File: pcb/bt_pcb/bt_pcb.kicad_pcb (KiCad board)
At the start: 4 copper layers, 180 x 70 mm, 219 parts, among them IC1 LTC3621EMS8E-25#PBF, IC2 ADAU1961WBCPZ-R7, IC3 STM32H750VBT6, IC4 STM32H523CEU6, IC5 W25Q512JVEIM, J1 Conn_01x02, J10 Conn_01x03, J11 Conn_01x03, J12 Conn_01x05, J13 Conn_01x05, J14 Conn_01x05, J15 ReanNYS216G, J16 ReanNYS216G, J17 ReanNYS216G, J18 ReanNYS216G, J2 694106301002, J3 Conn_01x01, J4 Conn_01x01, J5 Conn_01x03, J6 Conn_01x03, J7 ER-OLEDM0383-1-SPI_Conn_01x10, J8 Conn_01x03, J9 USB_C_Receptacle_USB2.0_16P, SW1 RotaryEncoder_Switch, SW10 SW_Push, SW11 SW_Push, SW2 SW_Push, SW3 SW_Push, SW4 SW_Push, SW5 SW_Push, SW6 SW_Push, SW7 SW_Push, SW8 SW_Push, SW9 SW_Push, U1 TLV76133DCY, U2 TLV76133DCY, U3 MCP6004, U4 MCP6004

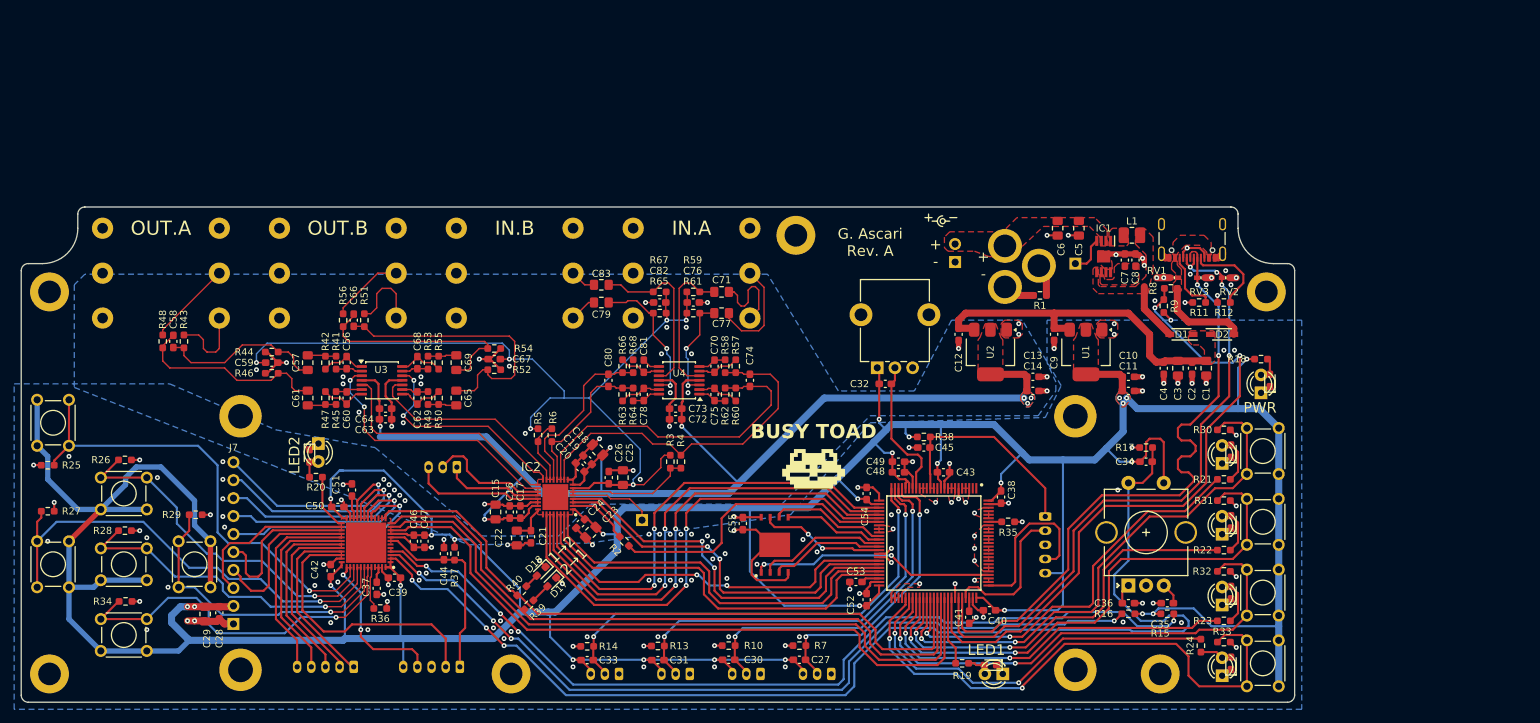
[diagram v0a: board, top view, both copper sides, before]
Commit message: redo of power supply
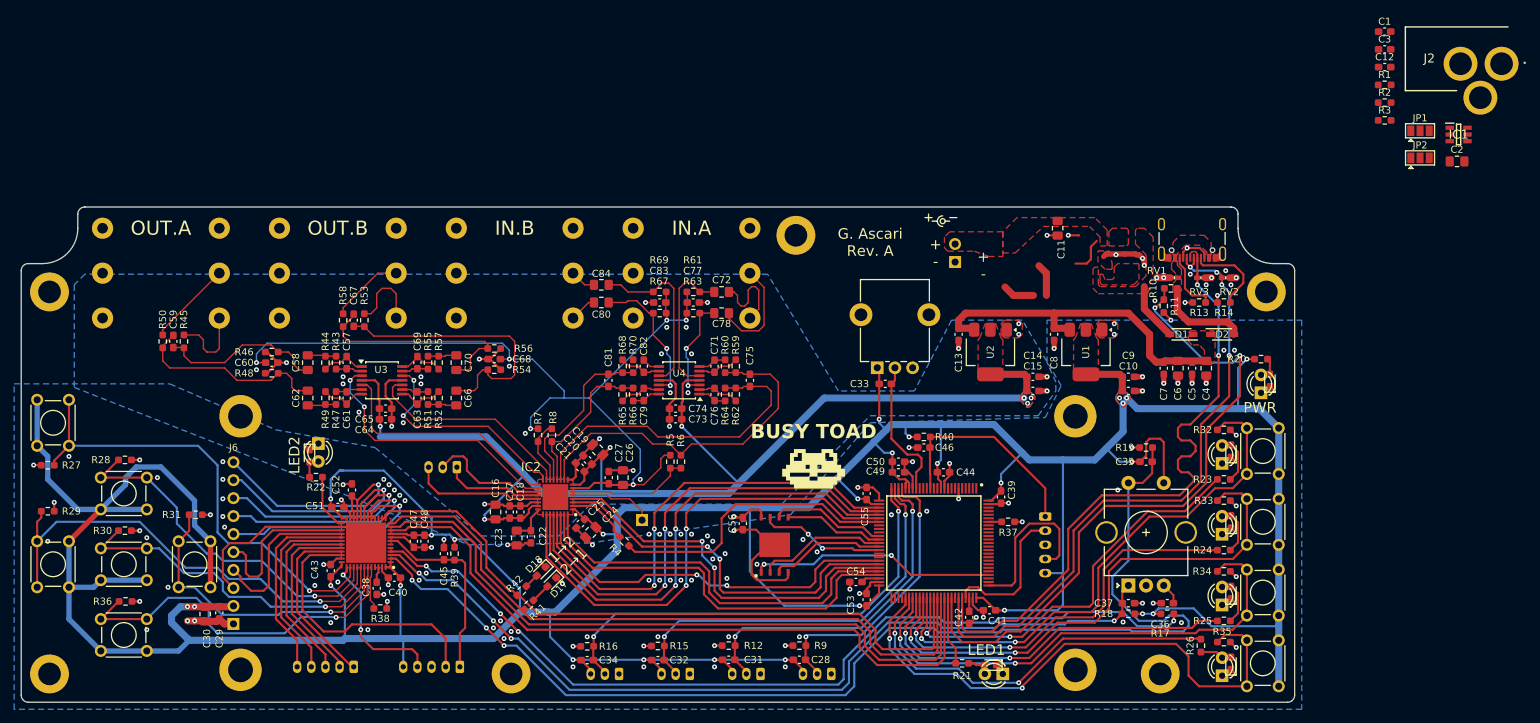
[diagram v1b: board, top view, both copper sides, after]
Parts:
- removed the C5 at (208.5, 52.0)
- removed the C7 at (215.0, 56.5)
- removed the C8 at (216.5, 56.5)
- removed the J3 at (208.0, 57.0)
- removed L1: 3.3u, Inductor_SMD:L_1008_2520Metric_Pad1.43x2.20mm_HandSolder
- added C1: 100n, Capacitor_SMD:C_0603_1608Metric_Pad1.08x0.95mm_HandSolder, F.Cu at (251.7, 24.2)
- added C12: 100n, Capacitor_SMD:C_0603_1608Metric_Pad1.08x0.95mm_HandSolder, F.Cu at (251.7, 29.2)
- added C2: 10u, Capacitor_SMD:C_0805_2012Metric_Pad1.18x1.45mm_HandSolder, F.Cu at (262.0, 42.6)
- added C3: 100n, Capacitor_SMD:C_0603_1608Metric_Pad1.08x0.95mm_HandSolder, F.Cu at (251.7, 26.7)
- added JP1: SJ+, Jumper:SolderJumper-3_P1.3mm_Open_Pad1.0x1.5mm, F.Cu at (256.7, 38.2)
- added JP2: SJ-, Jumper:SolderJumper-3_P1.3mm_Open_Pad1.0x1.5mm, F.Cu at (256.7, 42.1)
- added R2: 47k, Resistor_SMD:R_0603_1608Metric_Pad0.98x0.95mm_HandSolder, F.Cu at (251.7, 34.2)
- added R3: 47k, Resistor_SMD:R_0603_1608Metric_Pad0.98x0.95mm_HandSolder, F.Cu at (251.7, 36.8)
- IC1: value LTC3621EMS8E-25#PBF -> LV3842XDBVR; footprint library:SOP65P490X110-9N -> library:SOT95P280X145-6N
- J2: value 694106301002 -> Barrel_Jack_Switch; moved to F.Cu
- R1: value 10k -> 100k
- moved R1 57.1 mm to (251.7, 31.7), turned to 0 degrees
- moved J2 54.7 mm to (254.7, 32.5), turned to 0 degrees
- moved IC1 53.1 mm to (262.2, 38.8), turned to 0 degrees
- renumbered C11 to C10, C6 to C11, C12 to C13, C13 to C14, C14 to C15, C15 to C16, C16 to C17, C17 to C18, C18 to C19, C19 to C20, C20 to C21, C21 to C22, C22 to C23, C23 to C24, C24 to C25, C25 to C26, C26 to C27, C27 to C28, C28 to C29, C29 to C30, C30 to C31, C31 to C32, C32 to C33, C33 to C34, C34 to C35, C35 to C36, C36 to C37, C37 to C38, C38 to C39, C1 to C4, C39 to C40, C40 to C41, C41 to C42, C42 to C43, C43 to C44, C44 to C45, C45 to C46, C46 to C47, C47 to C48, C48 to C49, C2 to C5, C49 to C50, C50 to C51, C51 to C52, C52 to C53, C53 to C54, C54 to C55, C55 to C56, C56 to C57, C57 to C58, C58 to C59, C3 to C6, C59 to C60, C60 to C61, C61 to C62, C62 to C63, C63 to C64, C64 to C65, C65 to C66, C66 to C67, C67 to C68, C68 to C69, C4 to C7, C69 to C70, C70 to C71, C71 to C72, C72 to C73, C73 to C74, C74 to C75, C75 to C76, C76 to C77, C77 to C78, C78 to C79, C9 to C8, C79 to C80, C80 to C81, C81 to C82, C82 to C83, C83 to C84, C10 to C9, J11 to J10, J12 to J11, J13 to J12, J14 to J13, J15 to J14, J16 to J15, J17 to J16, J18 to J17, J4 to J3, J5 to J4, J6 to J5, J7 to J6, J8 to J7, J9 to J8, J10 to J9, R8 to R10, R9 to R11, R10 to R12, R11 to R13, R12 to R14, R13 to R15, R14 to R16, R15 to R17, R16 to R18, R17 to R19, R18 to R20, R19 to R21, R20 to R22, R21 to R23, R22 to R24, R23 to R25, R24 to R26, R25 to R27, R26 to R28, R27 to R29, R28 to R30, R29 to R31, R30 to R32, R31 to R33, R32 to R34, R33 to R35, R34 to R36, R35 to R37, R36 to R38, R37 to R39, R2 to R4, R38 to R40, R39 to R41, R40 to R42, R41 to R43, R42 to R44, R43 to R45, R44 to R46, R45 to R47, R46 to R48, R47 to R49, R3 to R5, R48 to R50, R49 to R51, R50 to R52, R51 to R53, R52 to R54, R53 to R55, R54 to R56, R55 to R57, R56 to R58, R57 to R59, R4 to R6, R58 to R60, R59 to R61, R60 to R62, R61 to R63, R62 to R64, R63 to R65, R64 to R66, R65 to R67, R66 to R68, R67 to R69, R5 to R7, R68 to R70, R6 to R8, R7 to R9
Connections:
- C11 pad 1: Net-(IC1-RUN) -> /Power Supply/VIN
- IC1 pad 2: Net-(IC1-RUN) -> GND
- IC1 pad 3: Net-(IC1-RUN) -> Net-(IC1-FB)
- IC1 pad 4: Net-(IC1-PGOOD) -> /Power Supply/VIN
- IC1 pad 5: Net-(D1-A) -> /Power Supply/VIN
- J1 pad 1: GND -> /Power Supply/VIN
- J1 pad 2: Net-(IC1-RUN) -> Net-(J1-Pin_2)
- J2 pad 1: GND -> Net-(JP1-A)
- J2 pad 2: Net-(IC1-RUN) -> Net-(JP1-B)
- J2 pad 3: Net-(J2-GND_2) -> Net-(JP1-B)
- R1 pad 1: Net-(J2-GND_2) -> Net-(D1-A)
- R1 pad 2: GND -> Net-(IC1-FB)
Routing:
- net (no net): track 0.00 -> 10.0 mm
- net GND: track 202.0 -> 195.9 mm, vias 171 -> 158
- net Net-(IC1-PGOOD): track 5.40 -> 0.00 mm
- net Net-(J2-GND_2): track 4.64 -> 0.00 mm
- net ENC_A: track 121.0 -> 122.5 mm
- net +3V3: track 656.7 -> 658.1 mm
- added copper zone on F.Cu, net (none)
- added copper zone on F.Cu, net /Power Supply/VIN
- added copper zone on F.Cu, net Net-(J1-Pin_2)
- removed copper zone on F.Cu, net Net-(IC1-CB)
- removed copper zone on F.Cu, net Net-(IC1-RUN)

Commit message: made a bom
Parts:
- added L1: 18uH 1.5A, library:SRR6040A180M, F.Cu at (209.2, 55.2)
- added TP1: TestPoint, TestPoint:TestPoint_Pad_D1.0mm, F.Cu at (198.0, 95.5)
- added TP2: TestPoint, TestPoint:TestPoint_Pad_D1.0mm, F.Cu at (199.0, 97.2)
- added TP3: TestPoint, TestPoint:TestPoint_Pad_D1.0mm, F.Cu at (198.0, 99.0)
- added TP4: TestPoint, TestPoint:TestPoint_Pad_D1.0mm, F.Cu at (199.0, 100.8)
- C64, C73: footprint Capacitor_SMD:C_0603_1608Metric_Pad1.08x0.95mm_HandSolder -> Capacitor_SMD:C_0805_2012Metric_Pad1.18x1.45mm_HandSolder
- J2: moved to B.Cu
- moved JP1 72.7 mm to (188.5, 63.3), turned to -90 degrees
- moved JP2 66.2 mm to (193.2, 60.7), turned to -90 degrees
- moved J2 63.4 mm to (192.2, 44.0), turned to -90 degrees
- moved IC1 62.6 mm to (202.2, 56.5), turned to -90 degrees
- moved C12 59.1 mm to (201.5, 60.4), turned to -45 degrees
- moved R1 57.2 mm to (198.4, 52.5), turned to -90 degrees
- moved C1 55.7 mm to (203.8, 52.5), turned to -90 degrees
- moved R2 53.7 mm to (200.9, 51.5)
- moved R3 53.4 mm to (200.9, 53.2)
- moved C3 48.5 mm to (216.2, 59.8), turned to 180 degrees
- moved C2 48.3 mm to (216.0, 57.5), turned to 180 degrees
- moved C15 11.5 mm to (190.5, 75.2), turned to -90 degrees
- moved C11 11.3 mm to (200.2, 62.0), turned to -45 degrees
- moved C14 9.76 mm to (192.5, 75.2), turned to 90 degrees
- moved J1 6.36 mm to (196.5, 60.0), turned to 180 degrees
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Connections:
- IC3 pad 12: GND -> unconnected-(IC3-PH0-OSC_IN-Pad12)
- IC3 pad 13: GND -> unconnected-(IC3-PH1-OSC_OUT-Pad13)
- IC3 pad 15: GND -> unconnected-(IC3-PC0-Pad15)
- IC3 pad 16: GND -> unconnected-(IC3-PC1-Pad16)
- IC3 pad 17: GND -> unconnected-(IC3-PC2_C-Pad17)
- IC3 pad 3: GND -> unconnected-(IC3-PE4-Pad3)
- IC3 pad 33: GND -> unconnected-(IC3-PC5-Pad33)
- IC3 pad 34: GND -> unconnected-(IC3-PB0-Pad34)
- IC3 pad 35: GND -> unconnected-(IC3-PB1-Pad35)
- IC3 pad 4: GND -> unconnected-(IC3-PE5-Pad4)
- IC3 pad 41: GND -> unconnected-(IC3-PE11-Pad41)
- IC3 pad 42: GND -> unconnected-(IC3-PE12-Pad42)
- IC3 pad 5: GND -> unconnected-(IC3-PE6-Pad5)
- IC3 pad 51: GND -> unconnected-(IC3-PB12-Pad51)
- IC3 pad 52: GND -> unconnected-(IC3-PB13-Pad52)
- IC3 pad 53: GND -> unconnected-(IC3-PB14-Pad53)
- IC3 pad 54: GND -> unconnected-(IC3-PB15-Pad54)
- IC3 pad 69: GND -> unconnected-(IC3-PA10-Pad69)
- IC3 pad 7: GND -> unconnected-(IC3-PC13-Pad7)
- IC3 pad 77: GND -> unconnected-(IC3-PA15-Pad77)
- IC3 pad 78: GND -> unconnected-(IC3-PC10-Pad78)
- IC3 pad 8: GND -> unconnected-(IC3-PC14-OSC32_IN-Pad8)
- IC3 pad 80: GND -> unconnected-(IC3-PC12-Pad80)
- IC3 pad 81: GND -> unconnected-(IC3-PD0-Pad81)
- IC3 pad 82: GND -> unconnected-(IC3-PD1-Pad82)
- IC3 pad 83: GND -> Net-(IC3-PD2)
- IC3 pad 84: GND -> Net-(IC3-PD3)
- IC3 pad 85: GND -> Net-(IC3-PD4)
- IC3 pad 86: GND -> Net-(IC3-PD5)
- IC3 pad 87: GND -> unconnected-(IC3-PD6-Pad87)
- IC3 pad 88: GND -> unconnected-(IC3-PD7-Pad88)
- IC3 pad 89: GND -> unconnected-(IC3-PB3-Pad89)
- IC3 pad 9: GND -> unconnected-(IC3-PC15-OSC32_OUT-Pad9)
- IC3 pad 90: GND -> unconnected-(IC3-PB4-Pad90)
- IC3 pad 91: GND -> unconnected-(IC3-PB5-Pad91)
- IC3 pad 92: GND -> unconnected-(IC3-PB6-Pad92)
- IC3 pad 93: GND -> unconnected-(IC3-PB7-Pad93)
- IC3 pad 95: GND -> unconnected-(IC3-PB8-Pad95)
- IC3 pad 96: GND -> unconnected-(IC3-PB9-Pad96)
- IC3 pad 97: GND -> unconnected-(IC3-PE0-Pad97)
- IC3 pad 98: GND -> unconnected-(IC3-PE1-Pad98)
- IC4 pad 14: GND -> unconnected-(IC4-PA4-Pad14)
- IC4 pad 15: GND -> unconnected-(IC4-PA5-Pad15)
- IC4 pad 16: GND -> unconnected-(IC4-PA6-Pad16)
- IC4 pad 45: GND -> unconnected-(IC4-PB8-Pad45)
- IC4 pad 5: GND -> unconnected-(IC4-PH0-OSC_IN-Pad5)
- IC4 pad 6: GND -> unconnected-(IC4-PH1-OSC_OUT-Pad6)
- J1 pad 1: /Power Supply/VIN -> GND
- J1 pad 2: Net-(J1-Pin_2) -> /Power Supply/VIN
- JP2 pad 2: Net-(J1-Pin_2) -> GND
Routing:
- net Net-(D1-A): track 8.24 -> 36.7 mm
- net Net-(JP1-B): track 0.00 -> 22.2 mm
- net /Power Supply/VIN: track 0.00 -> 14.3 mm
- net +3.3VA: track 170.2 -> 158.5 mm
- net Net-(JP1-A): track 0.00 -> 10.4 mm
- net (no net): track 10.0 -> 0.00 mm
- net Net-(IC1-SW): track 0.00 -> 6.25 mm
- net Net-(IC1-FB): track 0.00 -> 5.91 mm
- net Net-(IC3-PD2): track 0.00 -> 4.43 mm
- net Net-(IC3-PD4): track 0.00 -> 3.57 mm
- net Net-(IC3-PD5): track 0.00 -> 3.53 mm
- net Net-(IC3-PD3): track 0.00 -> 2.47 mm
- net Net-(IC1-CB): track 0.00 -> 2.16 mm
- net POT_0: track 20.2 -> 22.2 mm
- net +3V3: track 658.1 -> 660.1 mm
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- added copper zone on F.Cu, net Net-(JP1-B)
- removed copper zone on F.Cu, net (none)
- removed copper zone on F.Cu, net Net-(D1-A)
- removed copper zone on F.Cu, net Net-(J1-Pin_2)

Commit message: seeing the end of the tunnel
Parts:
- added J10: Conn_01x03, Connector_JST:JST_PH_B3B-PH-K_1x03_P2.00mm_Vertical, B.Cu at (180.3, 67.8)
- C56: value 2.2 -> 2.2u
- moved TP1 0.25 mm to (198.2, 95.5)
- moved TP2 0.25 mm to (199.2, 97.2)
- moved TP3 0.25 mm to (198.2, 99.0)
- moved TP4 0.25 mm to (199.2, 100.8)
- renumbered J10 to J11, J11 to J12, J12 to J13, J13 to J14, J14 to J15, J15 to J16, J16 to J17, J17 to J18
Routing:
- net +3V3: track 660.1 -> 664.0 mm
- net POT_0: track 22.2 -> 25.9 mm
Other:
- board text added: "POT"

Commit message: font draft and picture on pcb
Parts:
- added G***: LOGO, LOGO, B.Cu at (151.5, 92.5)
